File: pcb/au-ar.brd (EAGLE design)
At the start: 65 x 45 mm, 79 parts, among them U1 TPD12S520DBTR, U2 TPD12S521DBTR

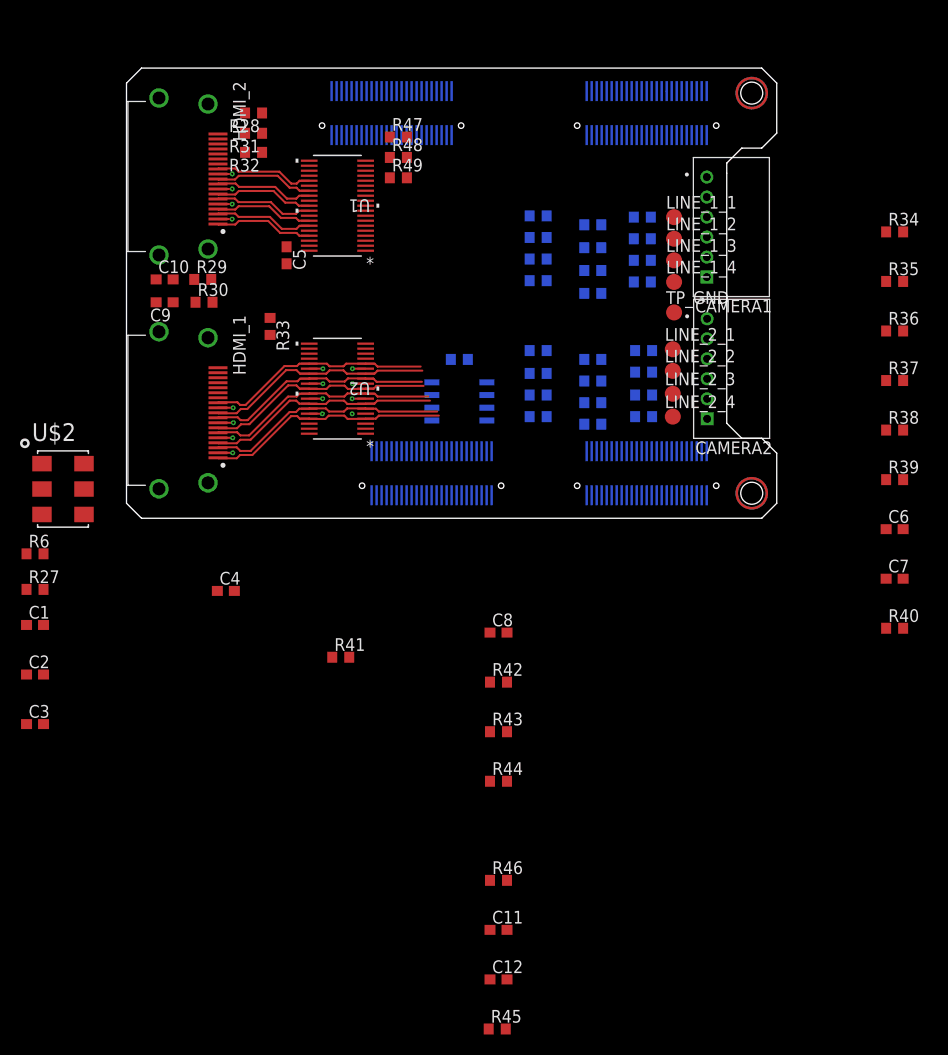
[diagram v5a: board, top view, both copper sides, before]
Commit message: reorganized hdmi pins, hdmi routing almost done
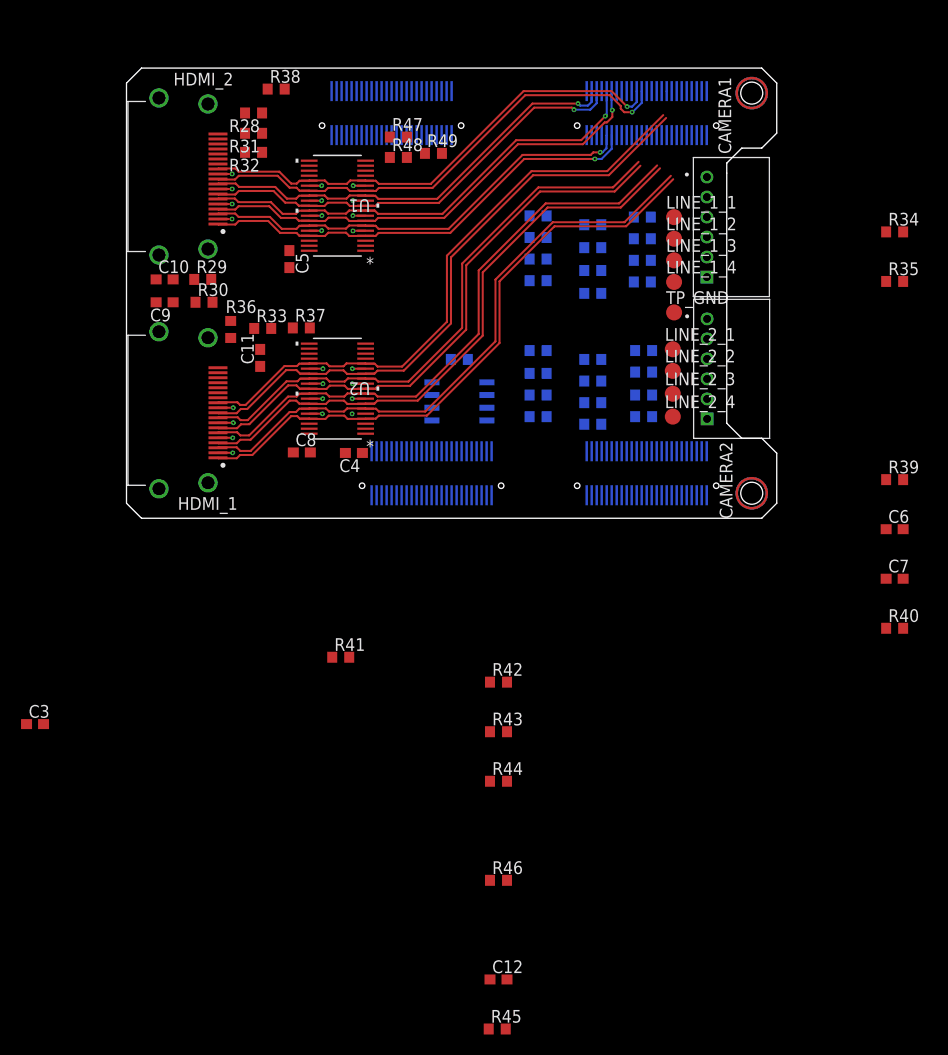
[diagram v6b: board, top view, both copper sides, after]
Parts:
- removed C1: 1uF, rcl:C0603
- removed C2: 0.1uF, rcl:C0603
- removed R27, R6: 3k, rcl:R0603
- removed U$2: SI514, lupa300-components:XTAL-6PIN
- moved R38 70.6 mm to (15.0, 42.9)
- moved R36 66.4 mm to (10.4, 18.9), turned to 270 degrees
- moved C11 61.9 mm to (13.4, 16.0), turned to 90 degrees
- moved R37 59.5 mm to (17.5, 19.0)
- moved C8 26.7 mm to (17.5, 6.58)
- moved C4 18.8 mm to (22.7, 6.53), turned to 180 degrees
- moved R49 4.27 mm to (30.7, 36.5)
- moved R33 0.76 mm to (13.6, 19.0), turned to 0 degrees
- moved C5 0.47 mm to (16.3, 25.9)
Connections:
- removed net EXT_CLK: B1.CB_45, U$2.P$4
- removed net SCL3: B1.CB_9, R27.1, U$2.P$2
- removed net SDA3: B1.CB_6, R6.1, U$2.P$1
- net 3V3: no longer C1.1, C2.1, R27.2, R6.2, U$2.P$6
- net D02_N: now also B1.BB_49; no longer B1.BB_11
- net D02_P: now also B1.BB_48; no longer B1.BB_12
- net D12_N: now also B1.BB_46; no longer B1.BB_37
- net D12_P: now also B1.BB_45; no longer B1.BB_36
- net D22_N: now also B1.BB_5; no longer B1.BB_14
- net D22_P: now also B1.BB_6; no longer B1.BB_15
- net GND: no longer C1.2, C2.2, U$2.P$3
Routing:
- net CLK2_P: track 9.92 -> 49.9 mm, vias 0 -> 1
- net CLK2_N: track 9.89 -> 48.8 mm, vias 0 -> 1
- net CLK1_P: track 22.8 -> 61.5 mm
- net CLK1_N: track 22.5 -> 61.0 mm
- net D12_P: track 9.88 -> 47.4 mm, vias 0 -> 1
- net D21_P: track 24.4 -> 61.2 mm
- net D21_N: track 24.2 -> 61.0 mm
- net D12_N: track 9.90 -> 46.6 mm, vias 0 -> 1
- net D11_P: track 23.5 -> 59.8 mm
- net D11_N: track 23.3 -> 59.5 mm
- net D22_P: track 9.90 -> 45.4 mm, vias 0 -> 1
- net D22_N: track 9.90 -> 44.7 mm, vias 0 -> 1
- net D02_P: track 9.90 -> 44.6 mm, vias 0 -> 1
- net D01_P: track 22.9 -> 57.5 mm
- net D01_N: track 22.7 -> 57.2 mm
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
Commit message: routed hdmi, need to route low speed signals
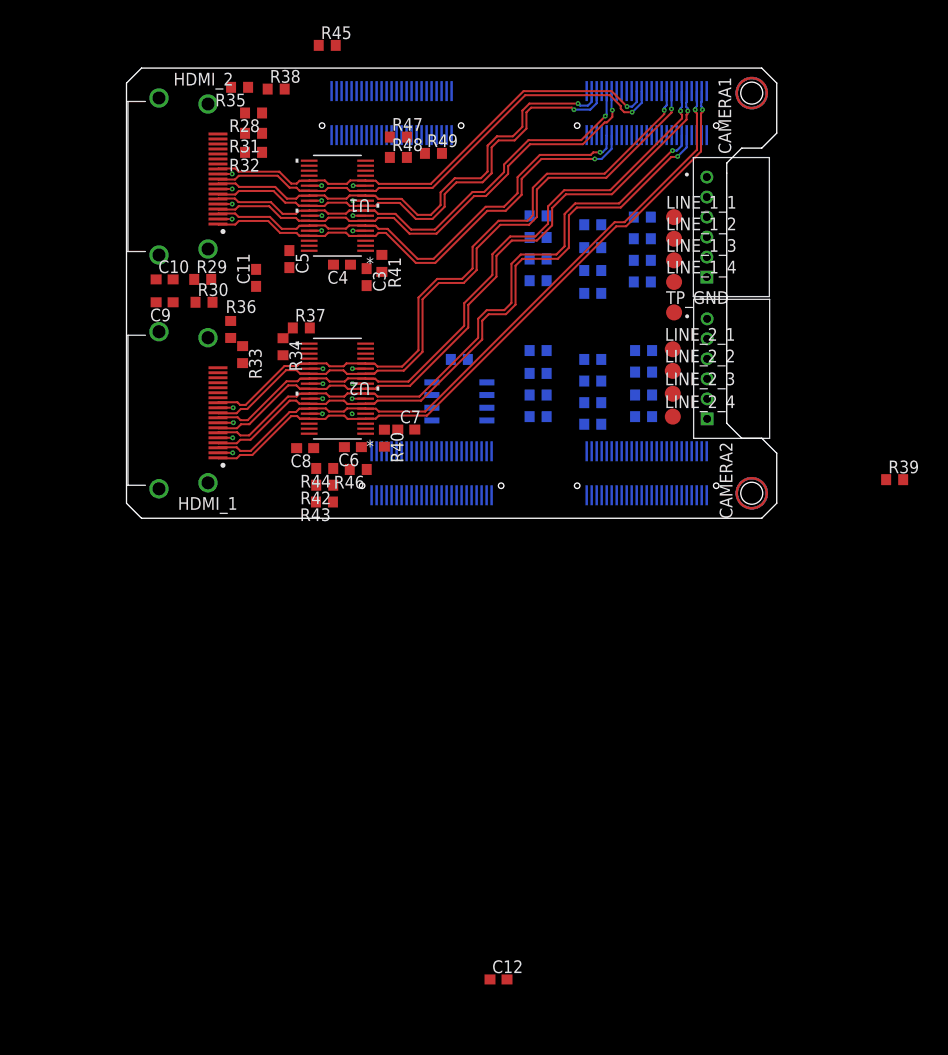
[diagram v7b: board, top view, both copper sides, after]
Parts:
- moved R45 99.8 mm to (20.1, 47.3)
- moved R35 68.3 mm to (11.3, 43.1), turned to 180 degrees
- moved R34 62.2 mm to (15.6, 17.1), turned to 270 degrees
- moved C3 55.6 mm to (24.0, 24.1), turned to 270 degrees
- moved C6 54.8 mm to (22.6, 7.11), turned to 180 degrees
- moved R40 54.4 mm to (25.8, 8.00), turned to 270 degrees
- moved C7 51.0 mm to (28.0, 8.86)
- moved R46 43.4 mm to (23.2, 4.88), turned to 180 degrees
- moved R41 39.6 mm to (25.5, 25.5), turned to 270 degrees
- moved R44 35.8 mm to (19.8, 4.98), turned to 180 degrees
- moved R43 28.8 mm to (19.8, 1.63), turned to 180 degrees
- moved R42 26.3 mm to (19.8, 3.30), turned to 180 degrees
- moved C4 18.9 mm to (21.5, 25.3)
- moved C11 8.01 mm to (13.0, 24.0)
- moved R33 3.30 mm to (11.6, 16.4), turned to 270 degrees
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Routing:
- net D01_P: track 57.5 -> 66.8 mm, vias 0 -> 1
- net D01_N: track 57.2 -> 66.0 mm, vias 0 -> 1
- net D21_P: track 61.2 -> 67.7 mm, vias 0 -> 1
- net D11_P: track 59.8 -> 66.2 mm, vias 0 -> 1
- net D21_N: track 61.0 -> 67.1 mm, vias 0 -> 1
- net D11_N: track 59.5 -> 65.4 mm, vias 0 -> 1
- net CLK1_P: track 61.5 -> 66.5 mm, vias 0 -> 1
- net CLK1_N: track 61.0 -> 65.7 mm, vias 0 -> 1
- net D02_N: track 43.8 -> 48.3 mm
- net D02_P: track 44.6 -> 49.1 mm
- net D22_P: track 45.4 -> 48.9 mm
- net D22_N: track 44.7 -> 48.1 mm
- net D12_N: track 46.6 -> 48.4 mm
- net D12_P: track 47.4 -> 49.2 mm

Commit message: added more routing
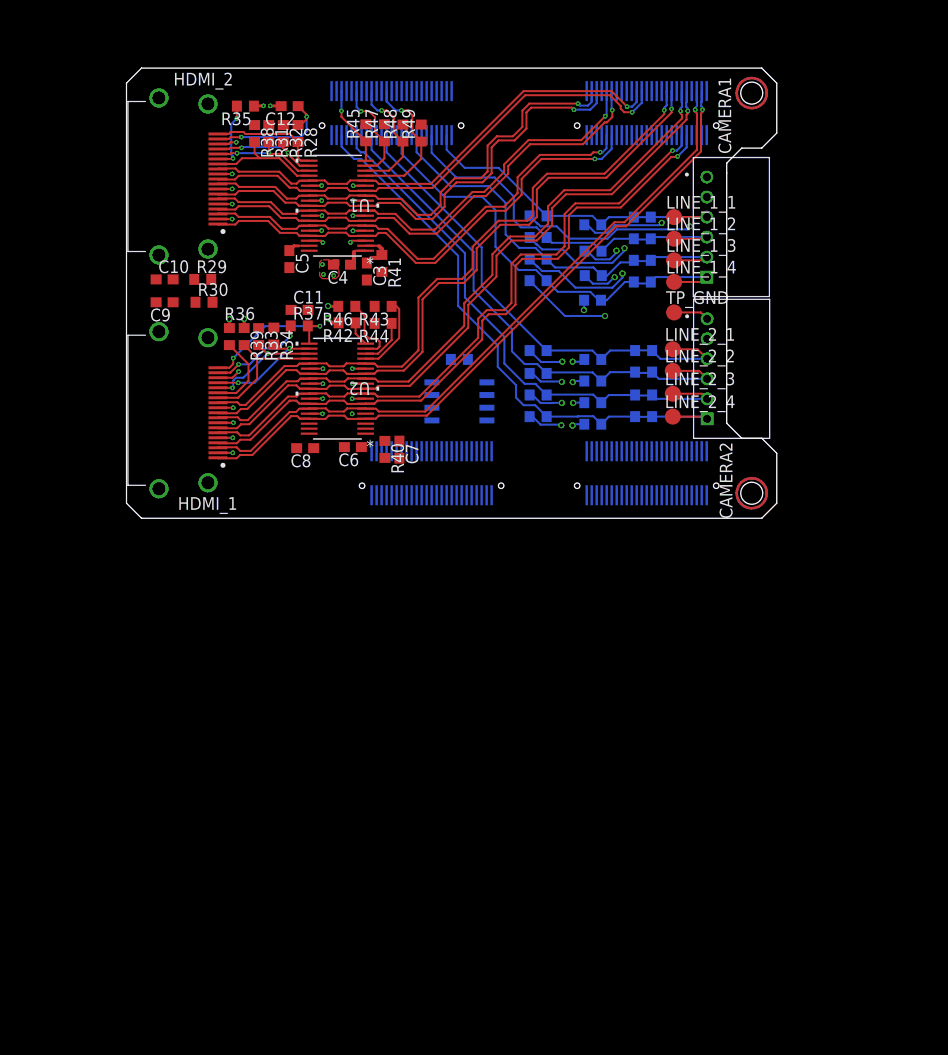
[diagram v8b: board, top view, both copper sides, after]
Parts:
- moved C12 89.8 mm to (16.3, 41.2), turned to 180 degrees
- moved R39 66.6 mm to (11.8, 18.2), turned to 270 degrees
- moved R43 20.4 mm to (25.7, 21.2)
- moved R42 16.4 mm to (22.0, 19.5)
- moved R46 16.3 mm to (22.0, 21.2)
- moved R44 15.6 mm to (25.7, 19.5)
- moved R45 9.55 mm to (23.9, 38.5), turned to 90 degrees
- moved C11 5.40 mm to (17.3, 20.8), turned to 0 degrees
- moved R38 4.94 mm to (12.8, 38.5), turned to 270 degrees
- moved R28 4.90 mm to (17.1, 38.5), turned to 270 degrees
- moved R32 3.52 mm to (15.7, 38.5), turned to 270 degrees
- moved R48 2.48 mm to (27.6, 38.5), turned to 90 degrees
- moved R33 2.41 mm to (13.2, 18.2)
- moved R49 2.37 mm to (29.5, 38.5), turned to 90 degrees
- moved C7 2.12 mm to (27.3, 6.86), turned to 270 degrees
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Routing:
- net GND: track 31.2 -> 108.4 mm, vias 24 -> 42
- net LINE_2_4: track 0.00 -> 47.2 mm
- net LINE_2_3: track 0.00 -> 44.2 mm
- net LINE_2_2: track 0.00 -> 41.4 mm
- net LINE_2_1: track 0.00 -> 37.7 mm
- net LINE_1_4: track 0.00 -> 34.1 mm
- net LINE_1_3: track 0.00 -> 31.0 mm
- net LINE_1_2: track 0.00 -> 28.0 mm
- net 3V3: track 0.00 -> 25.1 mm, vias 0 -> 11
- net LINE_1_1: track 0.00 -> 23.6 mm
- net HP1: track 0.00 -> 15.3 mm, vias 0 -> 2
- net CEC2_FPGA: track 0.00 -> 15.2 mm, vias 0 -> 1
- net CEC1: track 0.00 -> 13.8 mm
- net 5VHDMI2: track 0.00 -> 13.4 mm, vias 0 -> 2
- net SCL2_FPGA: track 0.00 -> 12.7 mm, vias 0 -> 1
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- added copper zone on layer 1, net GND
